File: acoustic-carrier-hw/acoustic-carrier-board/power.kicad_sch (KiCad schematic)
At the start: 28 parts, among them IC1 ECP5-BGA256, U6 TLV62569DRL, U7 TLV62569DRL, U8 TLV62569DRL

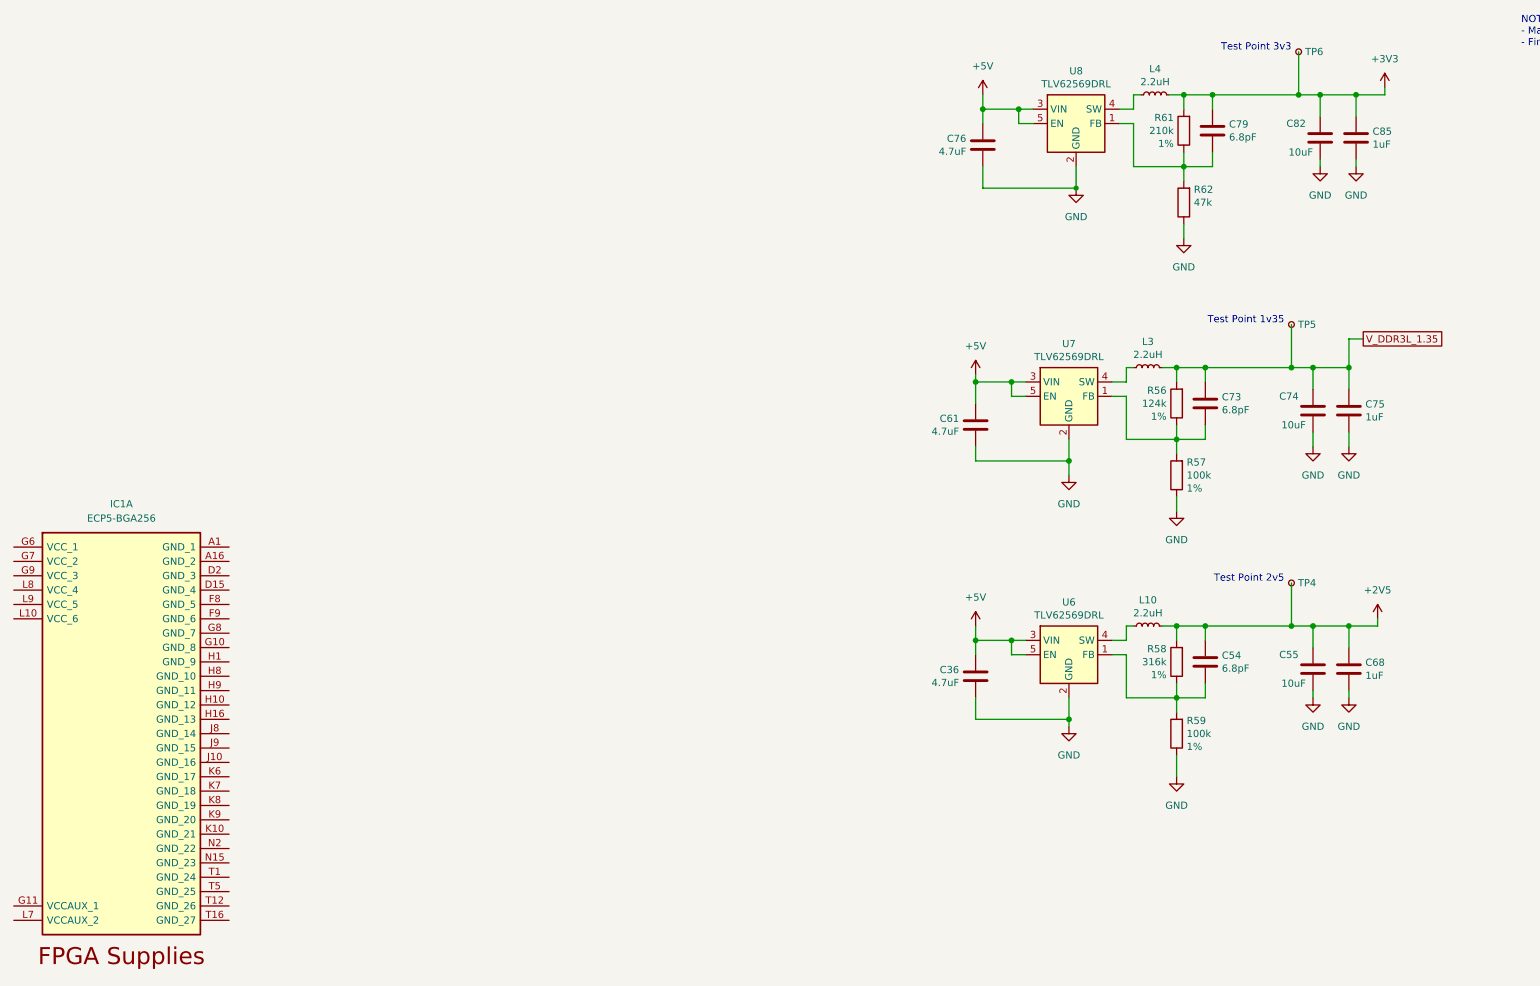
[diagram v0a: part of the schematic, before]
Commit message: [carrier] Added decoupling for DDR (next) Finish power supply
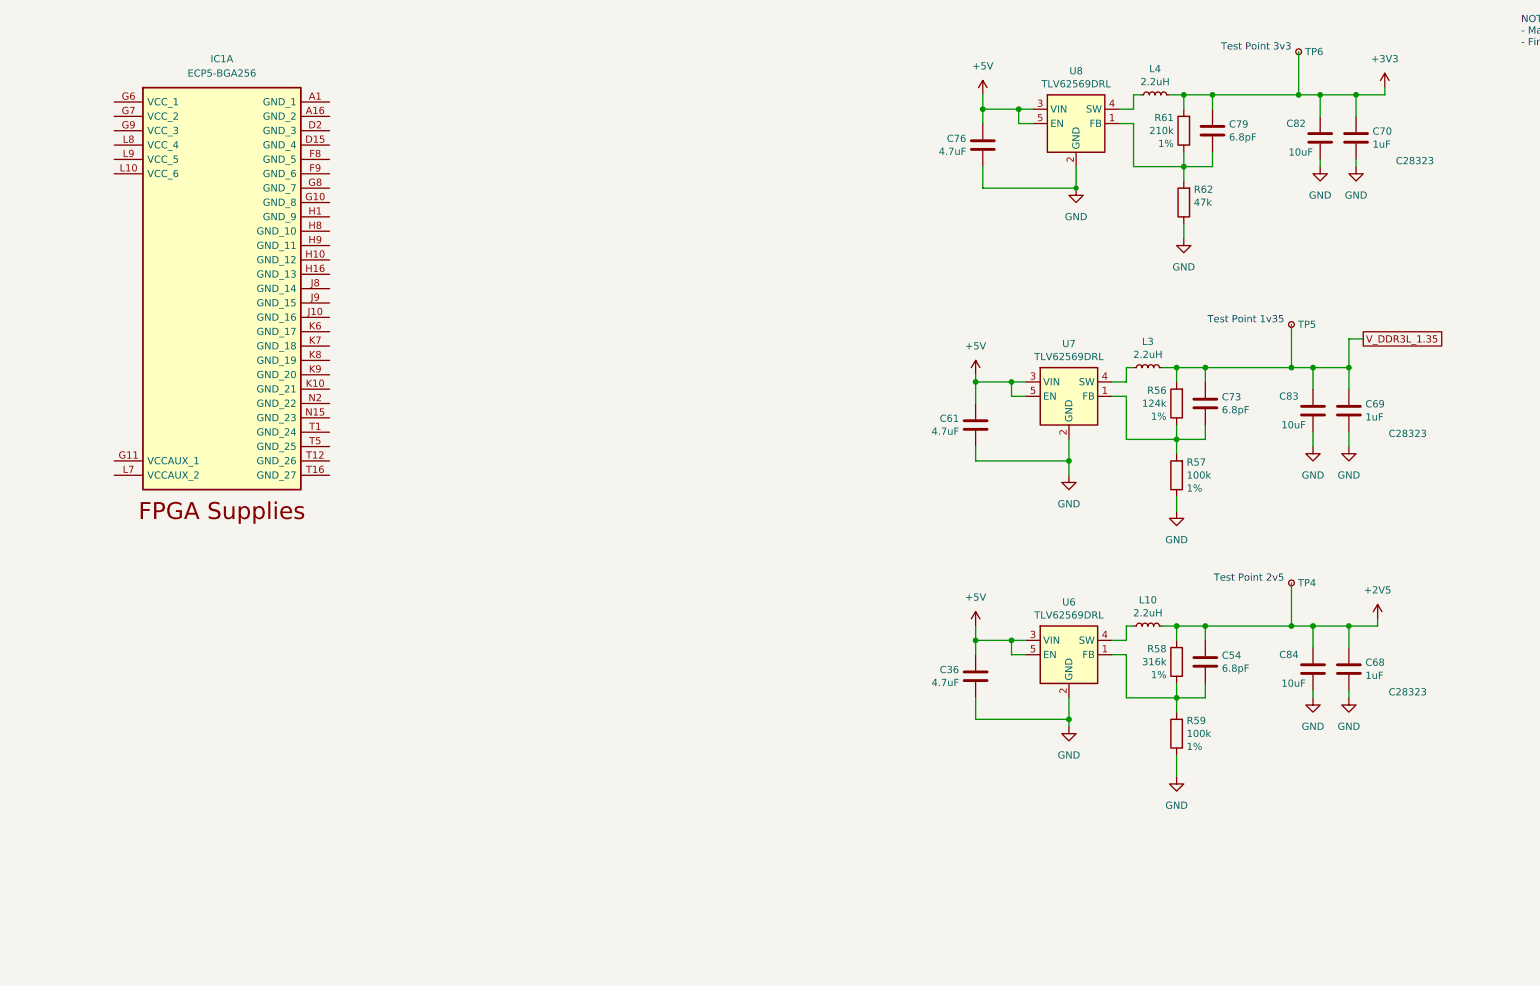
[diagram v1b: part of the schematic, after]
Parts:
- removed C55, C74: 10uF, Capacitor_SMD:C_0603_1608Metric, symbol Device:C
- removed C75, C85: 1uF, Capacitor_SMD:C_0402_1005Metric, symbol Device:C
- added C69, C70: 1uF, Capacitor_SMD:C_0805_2012Metric, symbol Device:C
- added C83, C84: 10uF, Capacitor_SMD:C_0603_1608Metric, symbol Device:C
- C68: footprint Capacitor_SMD:C_0402_1005Metric -> Capacitor_SMD:C_0805_2012Metric; LCSC Part Number (none) -> C28323; Manufacturing Part Number (none) -> CL21B105KBFNNNE; Mfg Yageo -> (none); PN CC0402KRX5R6BB105 -> (none)
- C82: LCSC Part Number (none) -> C19702; Manufacturing Part Number (none) -> CL10A106KP8NNNC; Mfg Yageo -> (none); PN CC0603KRX5R5BB106 -> (none)
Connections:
- net +2V5: now also C84.1
- net +3V3: now also C70.1
- net GND: now also C69.2, C70.2, C83.2, C84.2
- net V_DDR3L_1.35: now also C69.1, C83.1
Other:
- moved on the sheet: IC1A

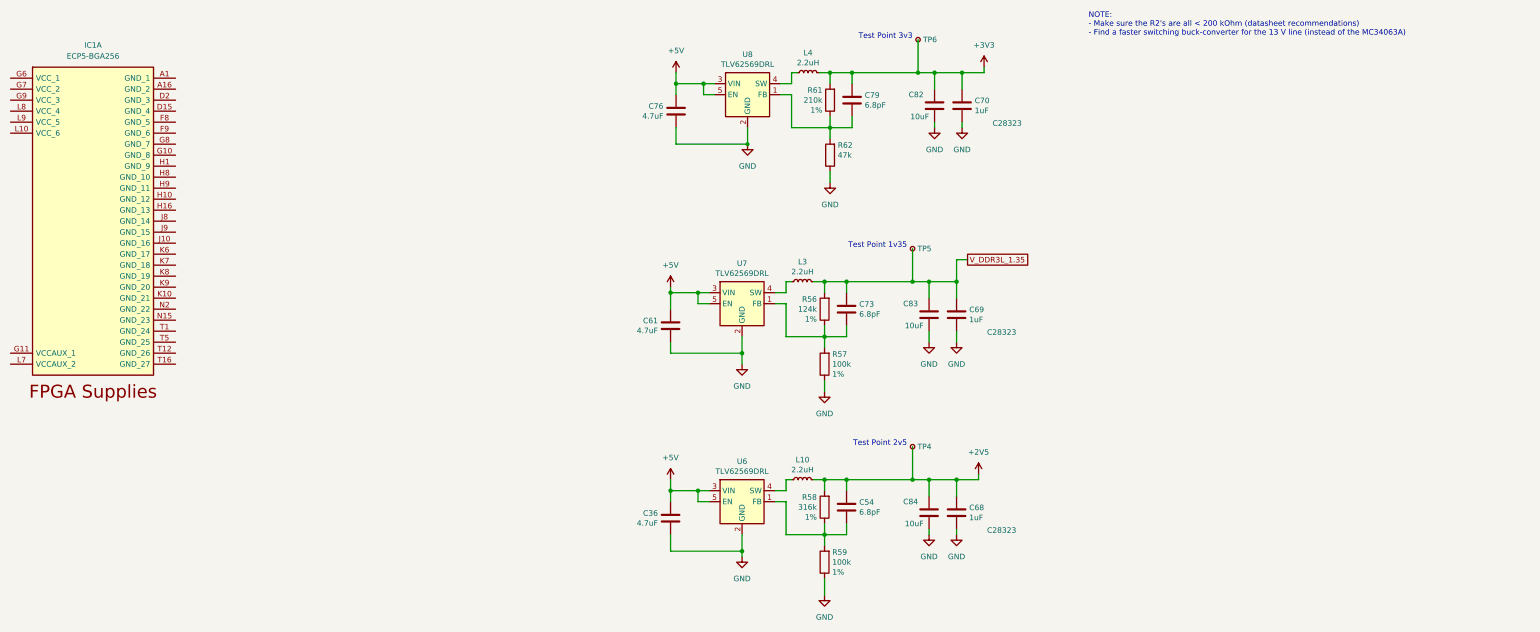
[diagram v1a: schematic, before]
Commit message: [carrier] Finished buck converters + simulations (next) Connect power to FPGA + add decoupling and bulk capacitance
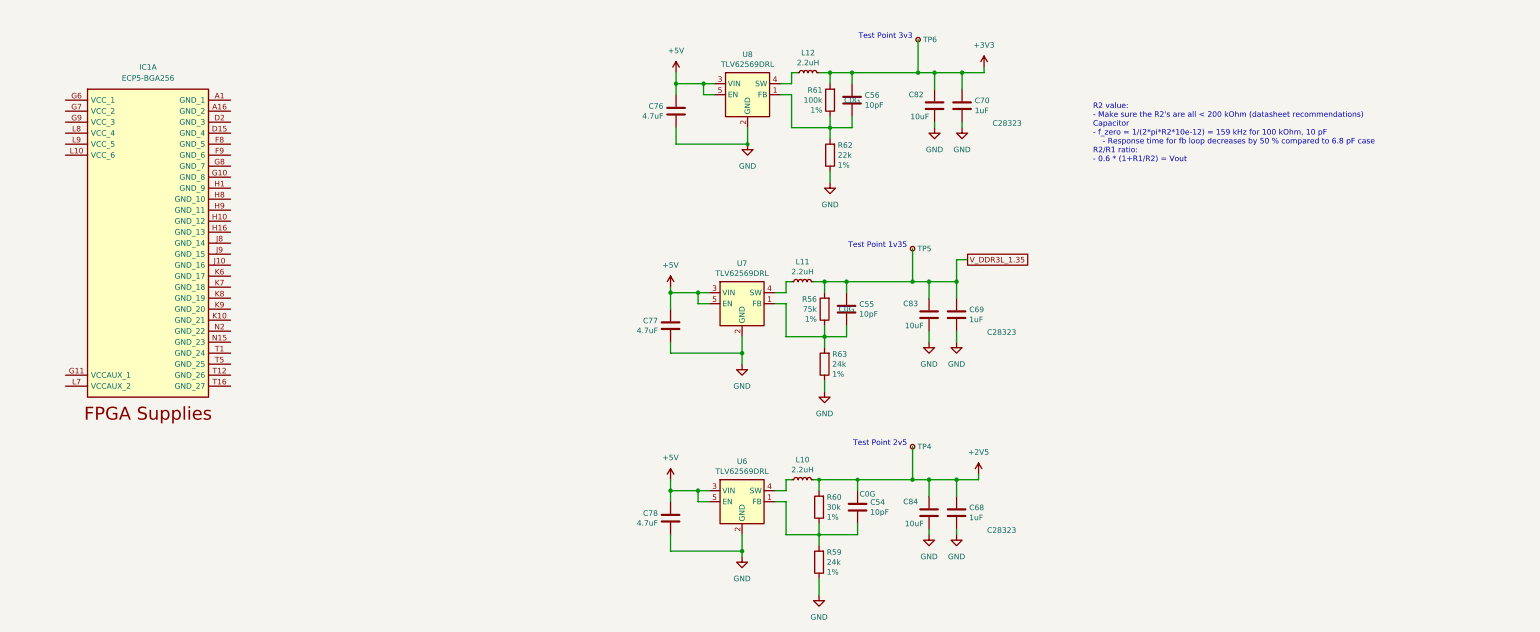
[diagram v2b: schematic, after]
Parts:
- removed C36, C61: 4.7uF, Capacitor_SMD:C_0402_1005Metric, symbol Device:C
- removed C73, C79: 6.8pF, Capacitor_SMD:C_0402_1005Metric, symbol Device:C
- removed L3, L4: 2.2uH, Inductor_SMD:L_0805_2012Metric, symbol Device:L_Small
- removed R57: 100k, Resistor_SMD:R_0402_1005Metric, symbol Device:R
- removed R58: 316k, Resistor_SMD:R_0402_1005Metric, symbol Device:R
- added C55, C56: 10pF, Capacitor_SMD:C_0402_1005Metric, symbol Device:C
- added C77, C78: 4.7uF, Capacitor_SMD:C_0402_1005Metric, symbol Device:C
- added L11, L12: 2.2uH, Inductor_SMD:L_0805_2012Metric, symbol Device:L_Small
- added R60: 30k, Resistor_SMD:R_0603_1608Metric, symbol Device:R
- added R63: 24k, Resistor_SMD:R_0603_1608Metric, symbol Device:R
- C54: value 6.8pF -> 10pF; LPN (none) -> C32949; MPN (none) -> CL05C100JB5NNNC; Mfg Yageo -> (none); PN CC0402CRNPO9BN6R8 -> (none)
- C76: LPN (none) -> C23733; MPN (none) -> CL05A475MP5NRNC; Mfg Yageo -> (none); PN CC0402KRX5R6BB475 -> (none)
- L10: LCSC Part Number (none) -> C28642347; Manufacturing Part Number (none) -> NR4018S2R2MT; Mfg Sunltech Tech -> (none); PN SLM20122R2MIT -> (none)
- R56: value 124k -> 75k; footprint Resistor_SMD:R_0402_1005Metric -> Resistor_SMD:R_0603_1608Metric; LPN (none) -> C23242; MPN (none) -> 0603WAF7502T5E; Mfg Yageo -> (none); PN RC0402FR-07124KL -> (none)
- R59: value 100k -> 24k; footprint Resistor_SMD:R_0402_1005Metric -> Resistor_SMD:R_0603_1608Metric; LPN (none) -> C23352; MPN (none) -> 0603WAF2402T5E; Mfg Yageo -> (none); PN RC0402FR-07100KL -> (none)
- R61: value 210k -> 100k; LPN (none) -> C25803; MPN (none) -> 0603WAF1003T5E; Mfg Yageo -> (none); PN RC0402FR-07210KL -> (none)
- R62: value 47k -> 22k; footprint Resistor_SMD:R_0402_1005Metric -> Resistor_SMD:R_0603_1608Metric; LPN (none) -> C31850; MPN (none) -> 0603WAF2202T5E; Mfg Yageo -> (none); PN RC0402FR-0747KL -> (none); Tol (none) -> 1%
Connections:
- net +2V5: now also R60.2
- net +3V3: now also C56.1, L12.2
- net +5V: now also C77.1, C78.1
- net GND: now also C77.2, C78.2, R63.1
- net V_DDR3L_1.35: now also C55.1, L11.2
- net at U7.4 (SW): now also L11.1
- net at U8.4 (SW): now also L12.1
- net at R56.1, U7.1 (FB): now also C55.2, R63.2
- net at C54.2, R59.2, U6.1 (FB): now also R60.1
- net at R61.1, R62.2, U8.1 (FB): now also C56.2
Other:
- note added: "R2 value: - Make sure the R2's are all < 200 kOhm (datasheet recommendations) Capacitor - f_zero = 1/(2*pi*R2*10e-12) = 159 kHz for 100 kOhm, 10 pF - Response time for fb loop decreases by 50 % compared to 6.8 pF case R2/R1 ratio: - 0.6 * (1+R1/R2) = Vout"
- note removed: "NOTE: - Make sure the R2's are all < 200 kOhm (datasheet recommendations) - Find a faster switching buck-converter for the 13 V line (instead of the MC34063A)"
- moved on the sheet: C54, IC1A, R59

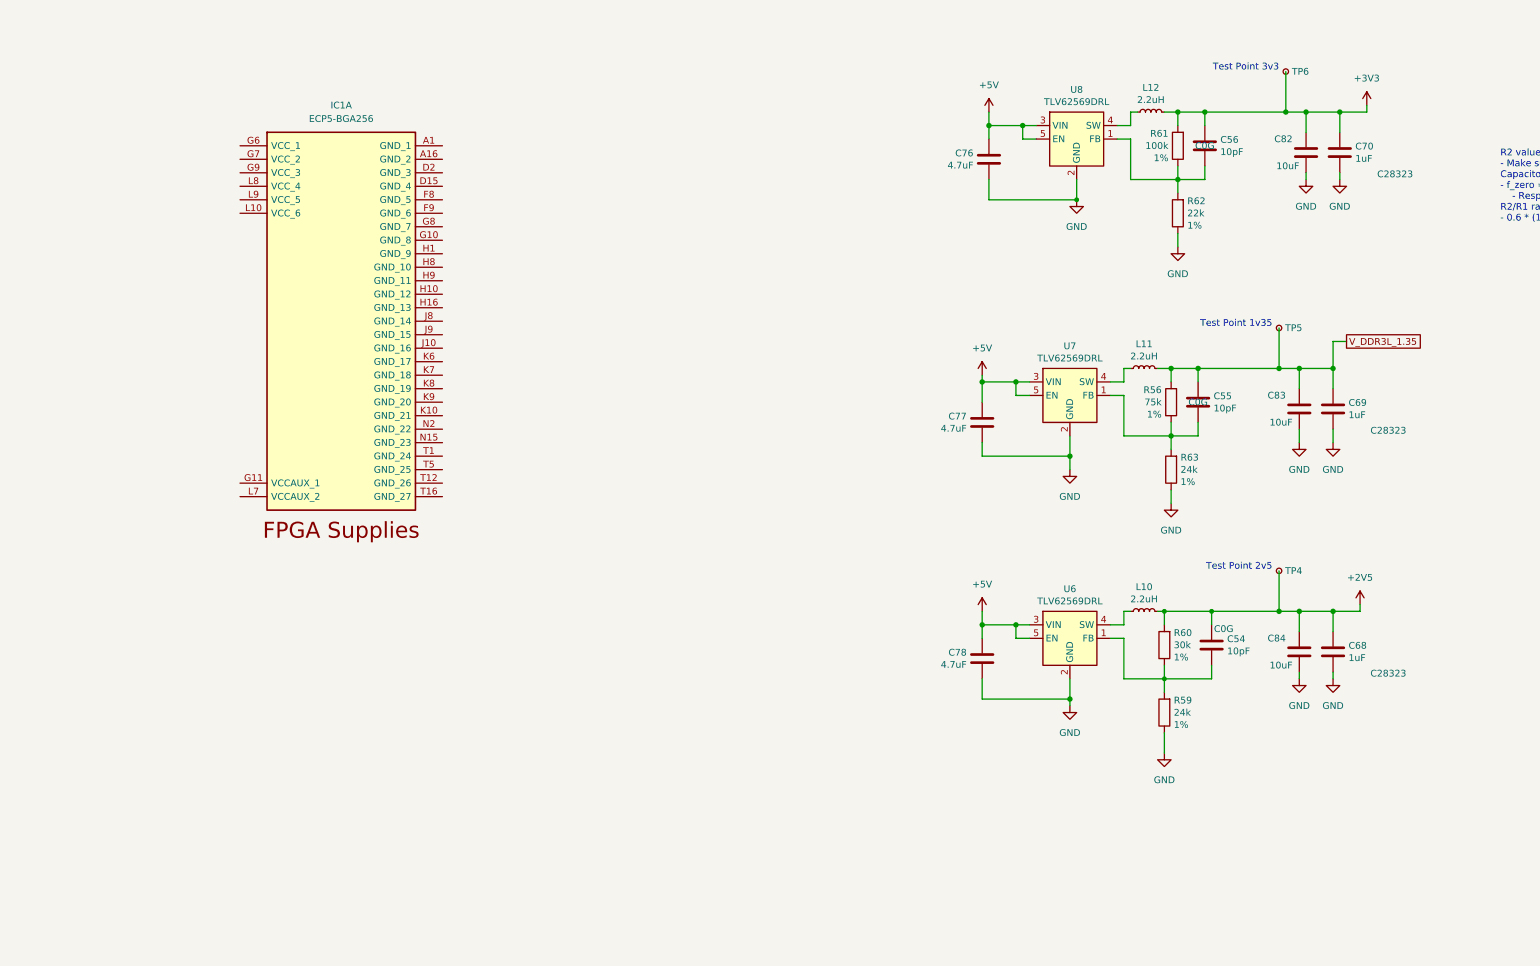
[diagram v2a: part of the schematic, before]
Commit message: added decoupling and power flags
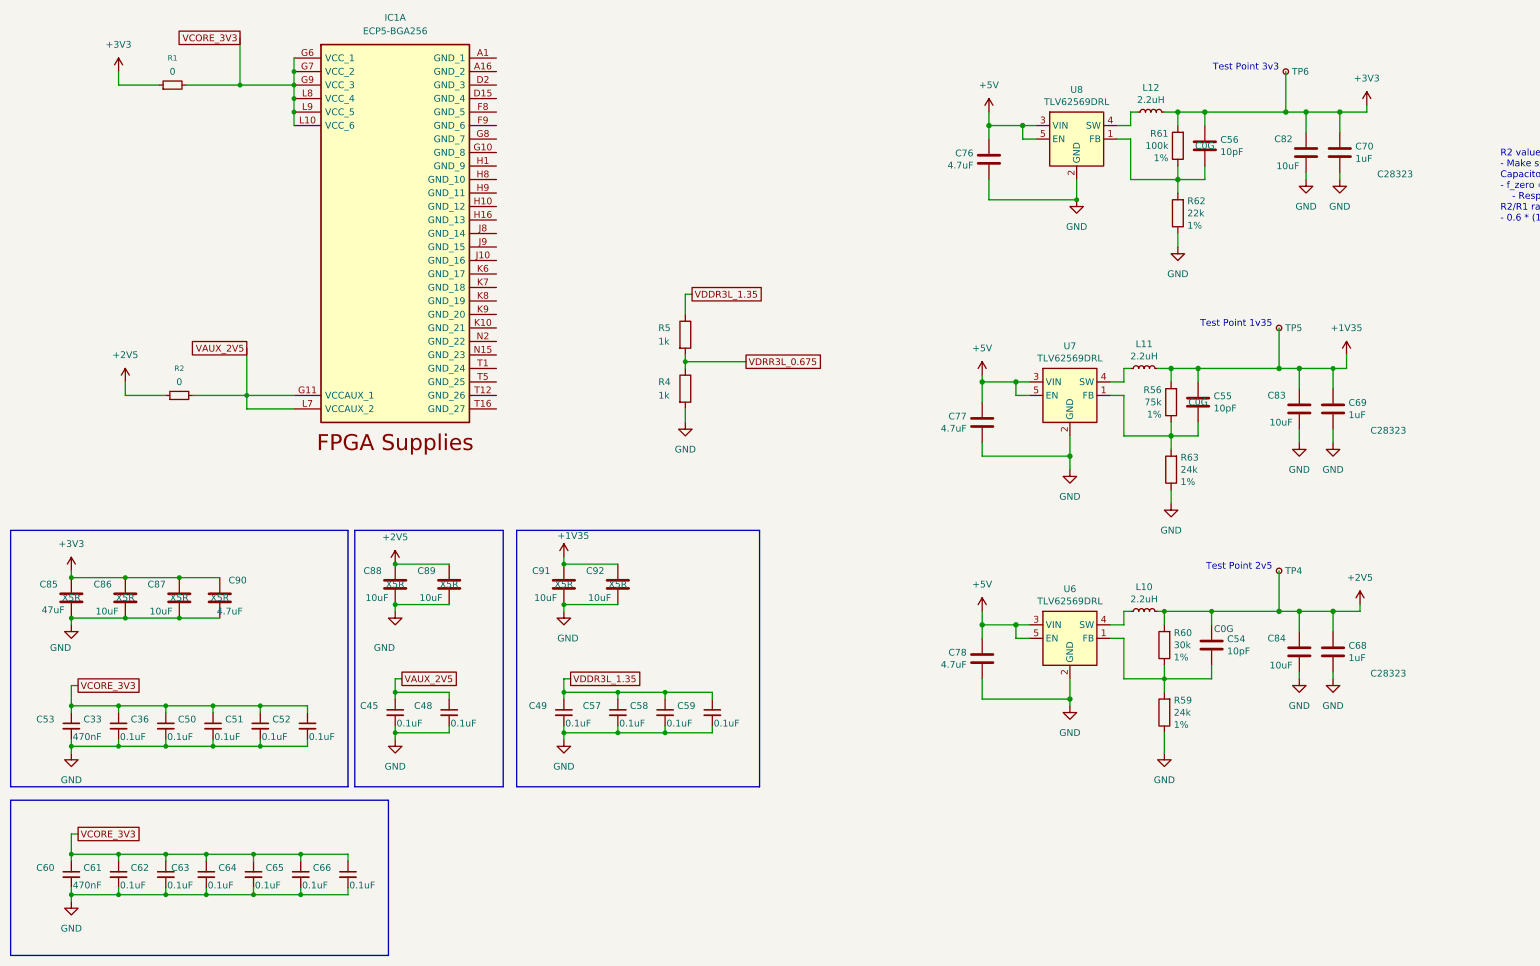
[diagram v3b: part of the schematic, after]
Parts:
- added C33, C36, C45, C48, C49, C50, C51, C52, C57, C58, C59, C61, C62, C63, C64, C65, C66: 0.1uF, Capacitor_SMD:C_0402_1005Metric, symbol Device:C_Small
- added C53, C60: 470nF, Capacitor_SMD:C_0603_1608Metric, symbol Device:C_Small
- added C85: 47uF, Capacitor_SMD:C_0805_2012Metric, symbol Device:C
- added C86, C87, C88, C89, C91, C92: 10uF, Capacitor_SMD:C_0603_1608Metric, symbol Device:C
- added C90: 4.7uF, Capacitor_SMD:C_0402_1005Metric, symbol Device:C
- added R1, R2: 0, Resistor_SMD:R_0805_2012Metric_Pad1.20x1.40mm_HandSolder, symbol Device:R_Small
- added R4, R5: 1k, Resistor_SMD:R_0805_2012Metric_Pad1.20x1.40mm_HandSolder, symbol Device:R
- IC1: footprint BGA256C80P16X16_1400X1400X170 -> (none)
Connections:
- net +2V5: now also C88.1, C89.1, R2.1
- net +3V3: now also C85.1, C86.1, C87.1, C90.1, R1.1
- net GND: now also C33.2, C36.2, C45.2, C48.2, C49.2, C50.2, C51.2, C52.2, C53.2, C57.2, C58.2, C59.2, C60.2, C61.2, C62.2, C63.2, C64.2, C65.2, C66.2, C85.2, C86.2, C87.2, C88.2, C89.2, C90.2, C91.2, C92.2, R4.2
- net VAUX_2V5: now reaches IC1.G11 (VCCAUX_1)
- net VAUX_2V5: now also IC1.L7 (VCCAUX_2), C45.1, C48.1, R2.2
- net VCORE_3V3: now reaches IC1.G6 (VCC_1)
- net VCORE_3V3: now also IC1.G7 (VCC_2), IC1.G9 (VCC_3), IC1.L10 (VCC_6), IC1.L8 (VCC_4), IC1.L9 (VCC_5), C33.1, C36.1, C50.1, C51.1, C52.1, C53.1, C60.1, C61.1, C62.1, C63.1, C64.1, C65.1, C66.1, R1.2
- net V_DDR3L_1.35 renamed +1V35
- net +1V35: now also C91.1, C92.1
- new net VDDR3L_1.35: C49.1, C57.1, C58.1, C59.1, R5.1
- new net VDRR3L_0.675: R4.1, R5.2
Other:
- moved on the sheet: IC1A
